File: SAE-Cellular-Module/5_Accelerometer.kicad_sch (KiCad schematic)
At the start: 9 parts, among them U6 BMI270

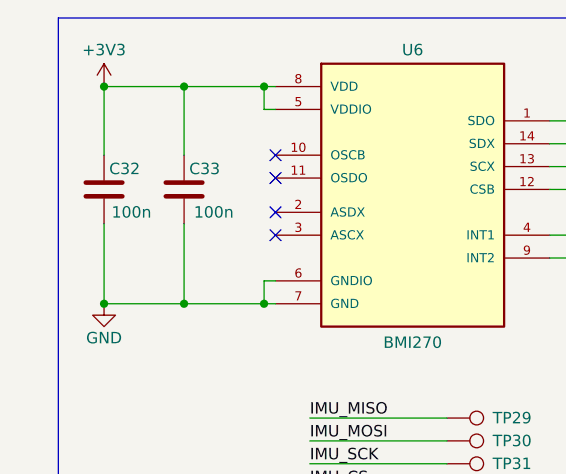
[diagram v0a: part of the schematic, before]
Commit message: Added initial component placements
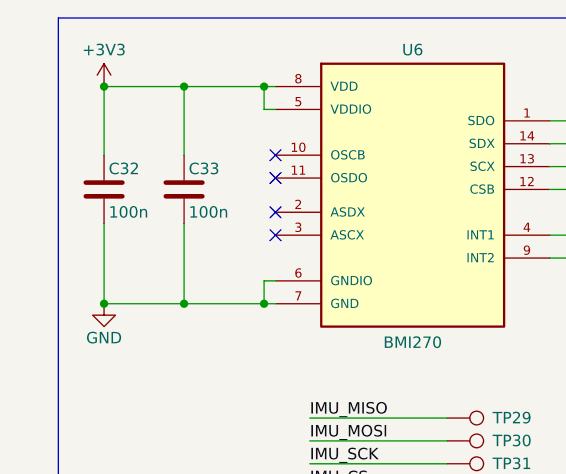
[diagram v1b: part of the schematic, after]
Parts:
- C32, C33: footprint (none) -> Capacitor_SMD:C_0402_1005Metric; MPN (none) -> CL05B104KP5NNNC
- TP29, TP30, TP31, TP32, TP33, TP34: footprint (none) -> TestPoint:TestPoint_Pad_D1.0mm
- U6: MPN (none) -> BMI270
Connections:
- net +3V3: now also C32.1, C33.1; no longer C32.2, C33.2
- net GND: now also C32.2, C33.2; no longer C32.1, C33.1
